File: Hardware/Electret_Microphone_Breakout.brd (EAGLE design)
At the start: 21.6 x 10.2 mm, 17 parts, among them M1 MIC9.7MM, U1 OPA344

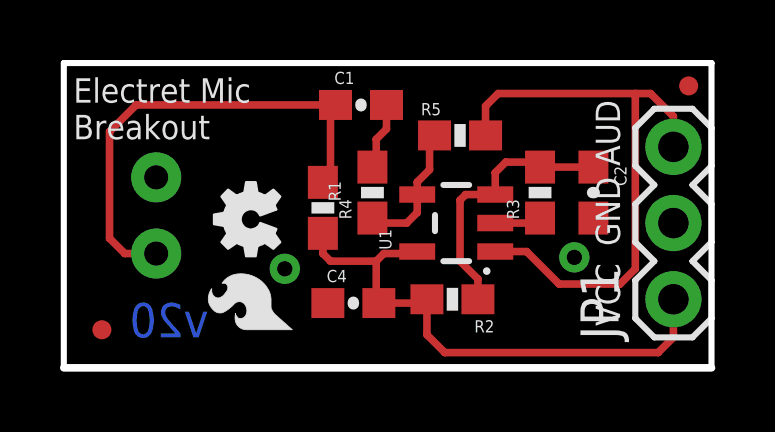
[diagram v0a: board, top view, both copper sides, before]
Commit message: Updated Board layout, removed 10 mils of board, went though DRU checklist
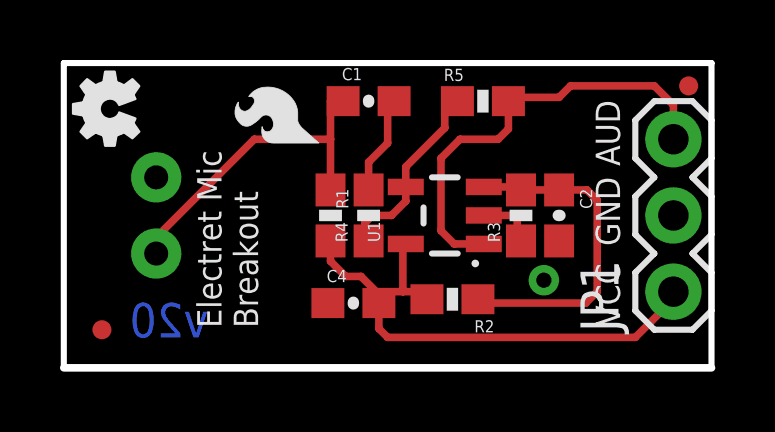
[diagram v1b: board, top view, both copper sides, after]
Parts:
- moved U$1 6.29 mm to (8.51, 7.49)
- moved LOGO1 5.97 mm to (1.52, 8.64)
- moved R5 1.37 mm to (14.0, 8.89)
- moved C2 1.37 mm to (16.5, 5.08)
- moved R3 0.99 mm to (15.2, 5.08)
- moved R4 0.77 mm to (10.2, 5.08)
- moved U1 0.46 mm to (12.7, 5.08)
- moved R1 0.36 mm to (8.89, 5.08)
- moved C1 0.28 mm to (10.2, 8.89)
- moved JP1 0.25 mm to (20.3, 2.54)
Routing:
- net AUD: track 19.9 -> 14.7 mm
- net N$1: track 16.0 -> 11.1 mm
- net N$7: track 9.02 -> 11.5 mm
- net N$2: track 4.52 -> 6.36 mm
- net N$6: track 2.27 -> 3.31 mm
- net GND: track 1.56 -> 1.94 mm, vias 2 -> 1

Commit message: Updated Board File--created room for bottom pin names
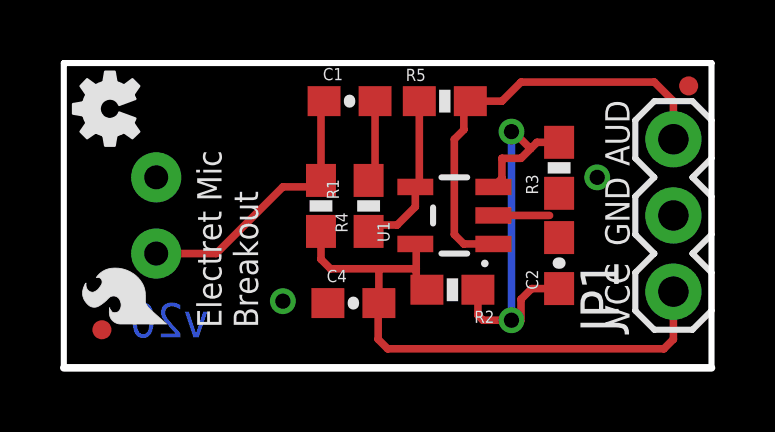
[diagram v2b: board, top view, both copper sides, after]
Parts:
- moved U$1 7.89 mm to (3.43, 1.46)
- moved R3 2.03 mm to (16.5, 6.67)
- moved C2 1.59 mm to (16.5, 3.49), turned to 90 degrees
- moved R5 1.27 mm to (12.7, 8.89)
- moved C1 0.63 mm to (9.53, 8.89)
- moved R1 0.45 mm to (8.57, 5.40)
- moved U1 0.32 mm to (13.0, 5.08)
- moved R2 0.32 mm to (13.0, 2.60)
- moved R4 0.32 mm to (10.2, 5.40)
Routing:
- net N$7: track 11.5 -> 14.8 mm, vias 0 -> 2
- net N$1: track 11.1 -> 9.19 mm
- net VCC: track 18.8 -> 20.0 mm
- net N$2: track 6.36 -> 5.47 mm
- net N$6: track 3.31 -> 2.73 mm
- net GND: track 1.94 -> 1.87 mm, vias 1 -> 2

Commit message: Moved logos around to look better
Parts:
- moved U$1 7.68 mm to (8.26, 7.43)

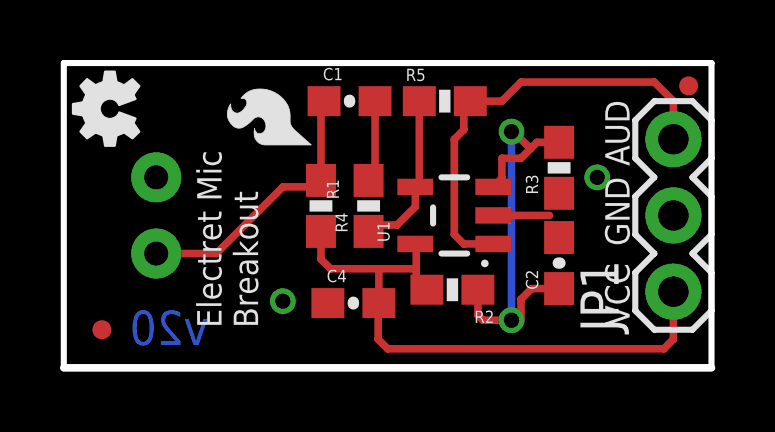
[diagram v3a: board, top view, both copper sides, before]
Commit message: Modified Baord per QC
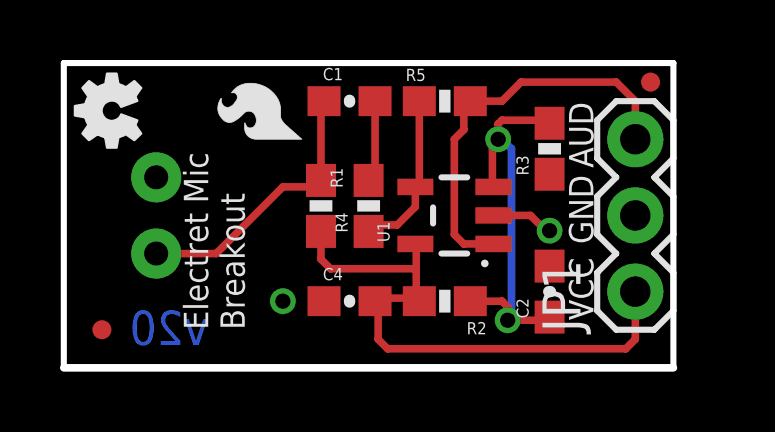
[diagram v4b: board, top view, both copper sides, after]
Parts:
- moved JP2 1.28 mm to (19.6, 9.53)
- moved JP1 1.27 mm to (19.1, 2.54)
- moved C2 1.00 mm to (16.2, 2.54)
- moved R3 0.71 mm to (16.2, 7.30)
- moved R2 0.46 mm to (12.7, 2.22)
- moved U$1 0.37 mm to (7.94, 7.62)
- moved C4 0.14 mm to (9.53, 2.22)
- moved LOGO1 0.09 mm to (1.59, 8.57)
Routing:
- net AUD: track 14.7 -> 13.4 mm
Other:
- board size 21.6 x 10.2 mm -> 20.3 x 10.2 mm
- board text added: "Nathan Seidle"

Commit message: Updated Board and Schematic per QC Review 2/12/2016
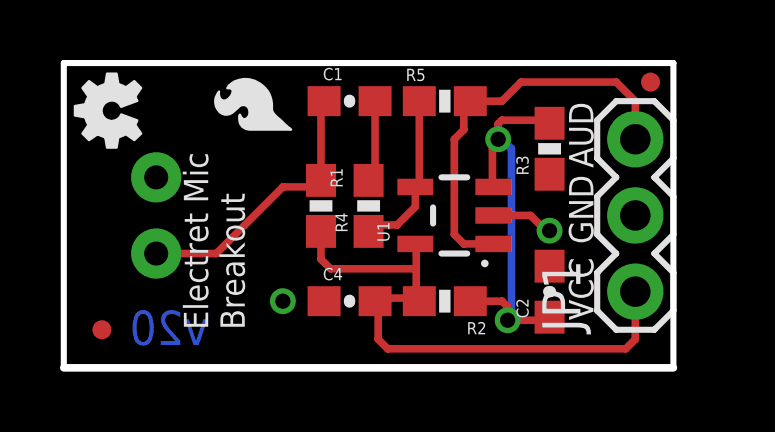
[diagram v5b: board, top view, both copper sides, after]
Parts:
- U$1: value LOGO-SFESK -> SFE_LOGO_FLAME.1_INCH; device SparkFun:SFE-LOGO-FLAME -> SparkFun-Aesthetics:SFE_LOGO_FLAME_.1
- moved U$2 31.4 mm to (4.06, -12.6)

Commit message: Updated Board File - updated MIC Package
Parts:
- MIC: value MIC9.7MM -> 9.7MM
- renumbered M1 to MIC
